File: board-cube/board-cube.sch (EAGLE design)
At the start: 164 parts, among them IC1 MSP430FR2110PW, IC2 LHA1+, IC3 MMZ09332BT1, Q1 BSS84, U1 TPS79933QDDCRQ1, U2 TPS79933QDDCRQ1, X1 BU-SMA-V, X10 BU-SMA-V, X11 BU-SMA-V, X12 BU-SMA-V, X13 BU-SMA-V, X14 BU-SMA-V, X15 BU-SMA-V, X16 BU-SMA-V, X17 BU-SMA-V, X2 BU-SMA-V, X3 BU-SMA-V, X4 BU-SMA-V, X5 BU-SMA-V, X6 BU-SMA-V, X7 BU-SMA-V, X8 BU-SMA-V, X9 BU-SMA-V

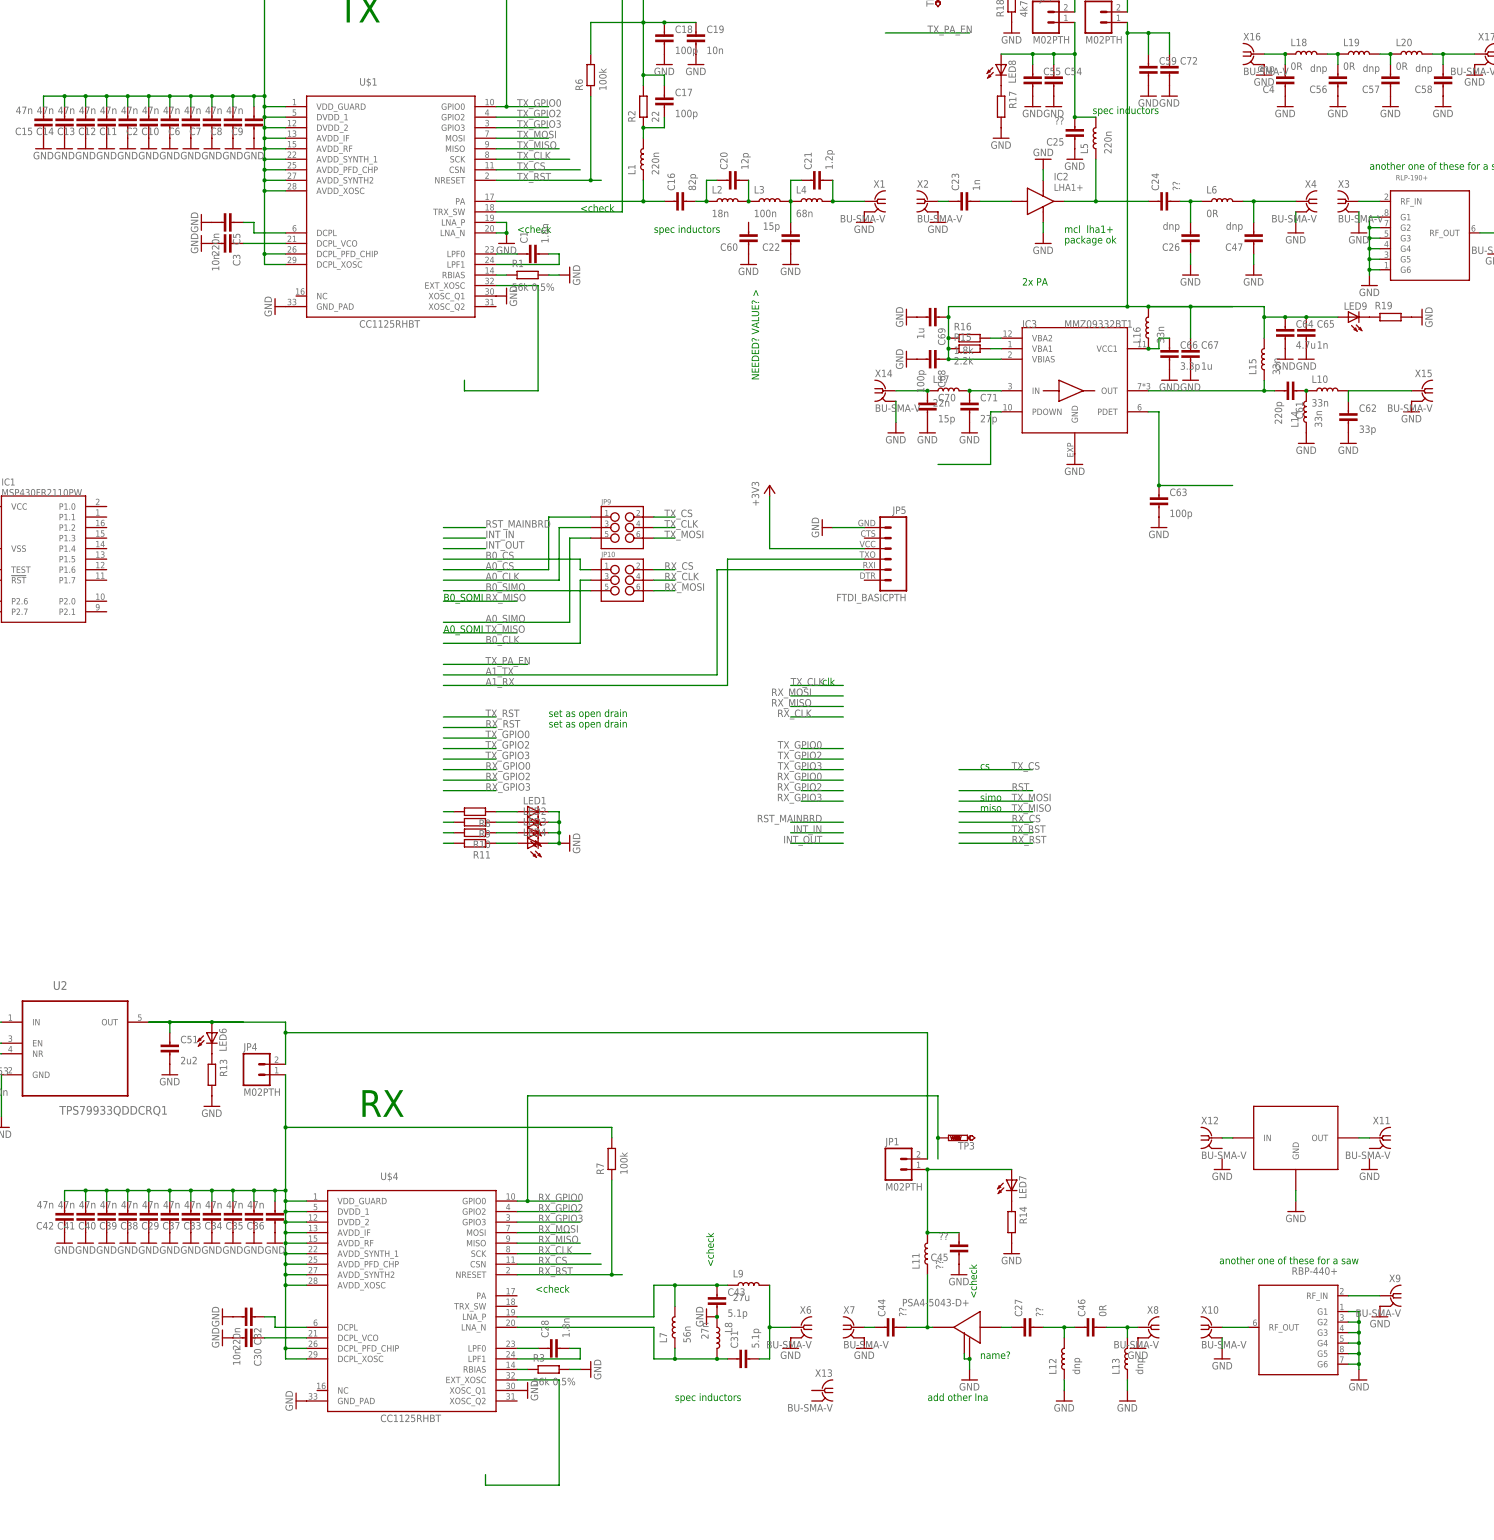
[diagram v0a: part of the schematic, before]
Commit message: adding tcxo and temp sensor
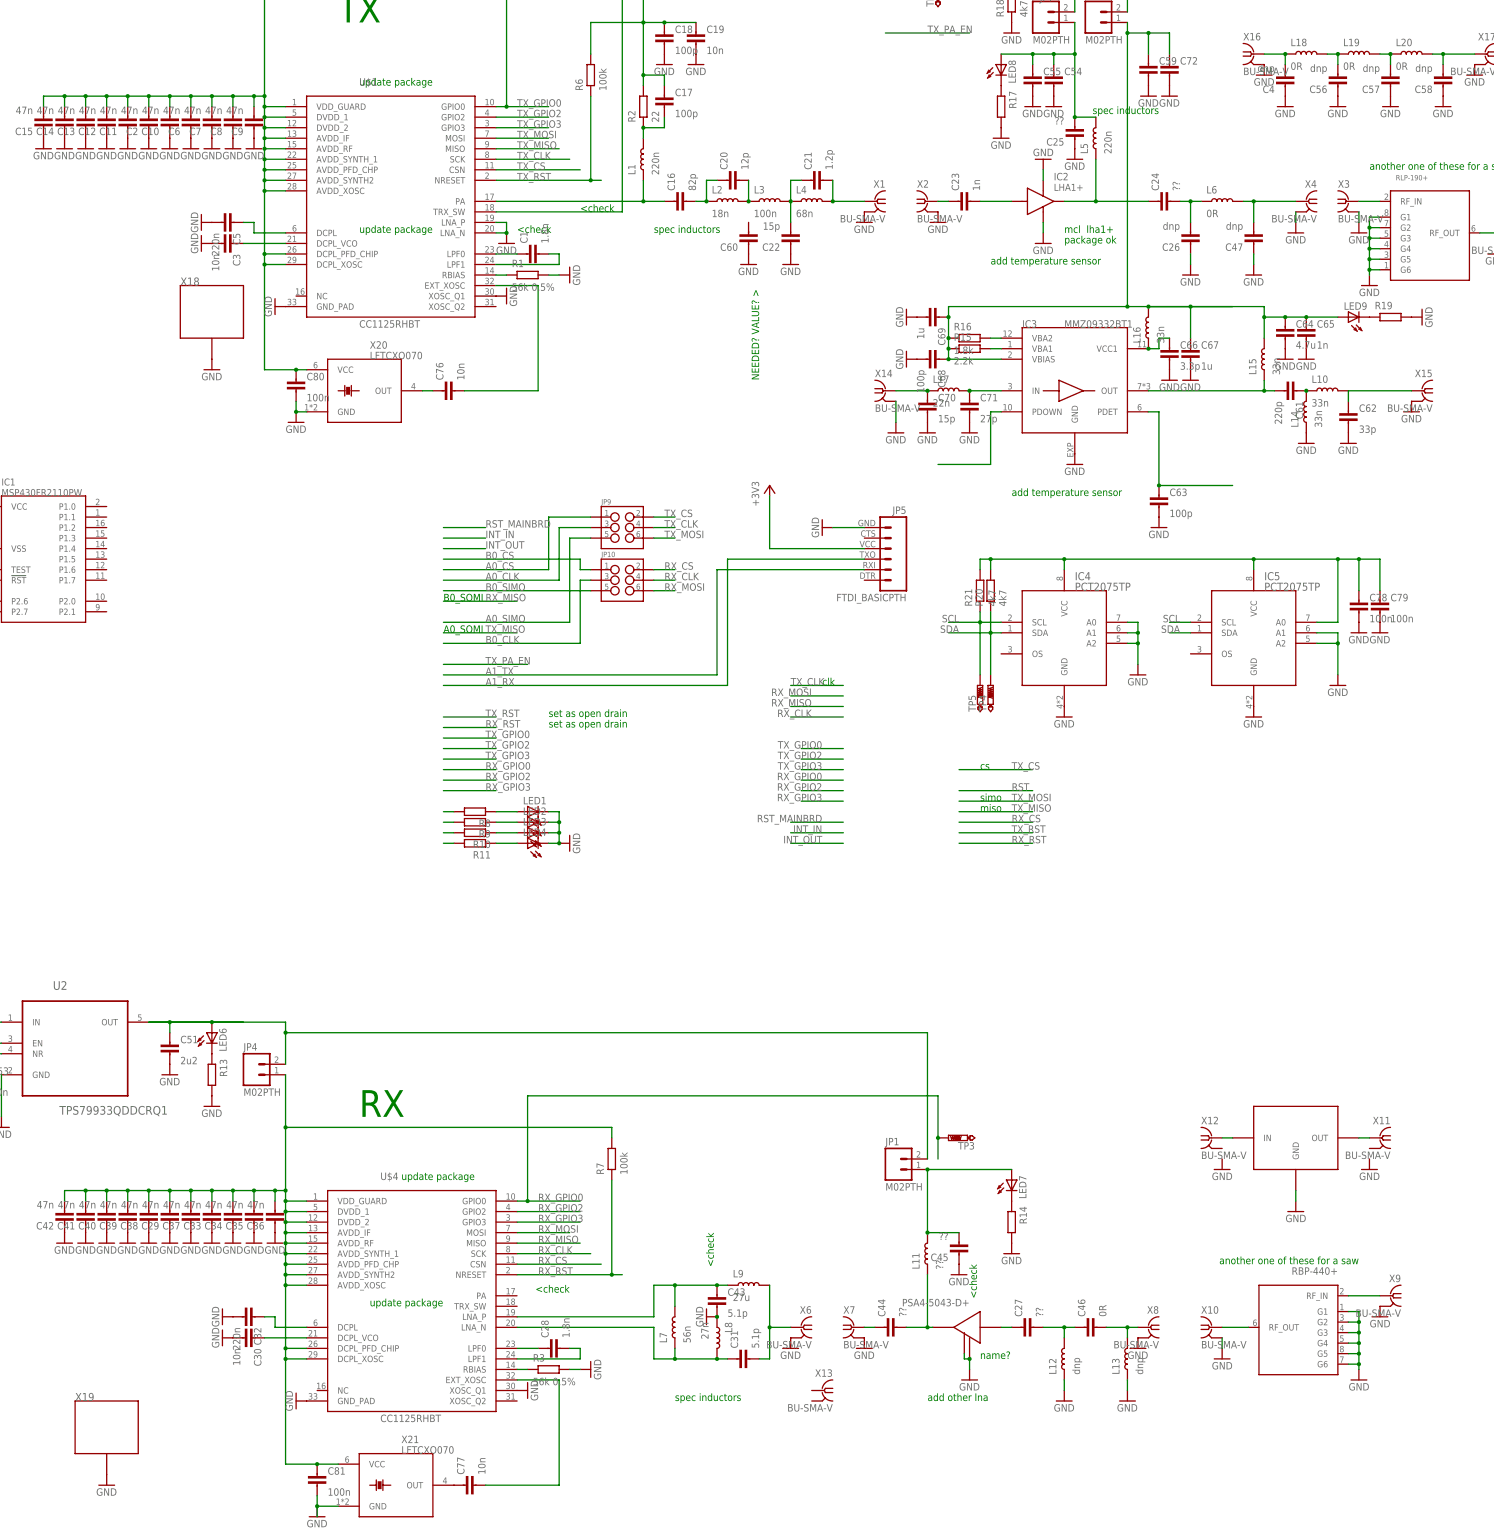
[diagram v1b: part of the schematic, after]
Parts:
- added C76, C77: 10n, passives-7351:CAPACITOR0603-N
- added C78, C79, C80, C81: 100n, passives-7351:CAPACITOR0603-N
- added IC4, IC5: PCT2075TP, CubeSat3:PCT2075TP
- added R20, R21: 4k7, passives-7351:RESISTOR0603-N
- added TP4, TP5: PTR1B1,27, testpad:PTR1B1,27
- added X18, X19: SHIELD-26X26, CubeSat3:SHIELD-26X26
- added X20, X21: LFTCXO070, CubeSat3:LFTCXO070
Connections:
- new net N$81: C76.1, X20.OUT
- new net N$82: C77.1, X21.OUT
- new net N$86: C78.1, C79.1, IC4.VCC, IC5.A0, IC5.VCC, R20.P$2, R21.P$2
- new net SCL: IC4.SCL, IC5.SCL, R21.P$1, TP5.TP
- new net SDA: IC4.SDA, IC5.SDA, R20.P$1, TP4.TP
- net GND: now also C78.2, C79.2, C80.2, C81.2, IC4.A0, IC4.A1, IC4.A2, IC4.GND, IC5.A1, IC5.A2, IC5.GND, X18.G, X19.G, X20.GND, X21.GND
- net N$36: now also C77.2
- net N$51: now also C80.1, X20.VCC
- net N$63: now also C81.1, X21.VCC
- net N$9: now also C76.2
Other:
- note added: "add temperature sensor"
- note added: "update package"
- note removed: "2x PA"

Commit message: updating footprints and values, changing msp watchdog part
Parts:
- removed IC1: MSP430FR2110PW, CubeSat3:MSP430FR2110PW
- added C82: (no value), passives-7351:CAPACITOR0603-N
- added IC6: MSP430FR2311PW, CubeSat3:MSP430FR2311PW
- added JP11: FTDI_BASICPTH, SparkFun-Connectors:FTDI_BASICPTH
- added JP8: (no value), SparkFun-Connectors:M04PTH
- added L21: 15n, passives-7351:INDUCTOR0603-N
- C60: value (none) -> 12p
- renumbered U$1 to IC7, U$3 to FL1, U$4 to IC8, U$6 to FL2, U$7 to FL3
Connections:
- new net N$83: IC6.TEST, JP8.4
- new net N$84: IC6.!RST, JP8.3
- new net N$85: IC6.P1.6, JP11.3
- new net N$87: IC6.P1.7, JP11.2
- new net N$88: C82.1, L21.P$2
- new net N$89: L21.P$1
- new net N$90: C82.2
- net GND: now also IC6.VSS, JP11.6, JP8.2; no longer IC1.VSS
- net N$21: now also C60.2
- net N$80: now also IC6.VCC, JP8.1; no longer IC1.VCC
- net SCL: now also IC6.P1.3
- net SDA: now also IC6.P1.2
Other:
- note added: "12p"
- note added: "150n"
- note added: "15n"
- note added: "18"
- note added: "22n"
- note added: "2p2"
- note added: "39p"
- note added: "43n"
- note added: "56n"
- note added: "56p"
- note added: "5p1"
- note added: "6p2"
- note added: "82n"
- note added: "^ needed?"
- note added: "dnp"
- note added: "for test board only"
- note added: "green: 144 MHz"
- note added: "green: 434 MHz"
- note added: "make consistant"
- note removed: "NEEDED? VALUE? >"
- note removed: "update package"

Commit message: added level shifter
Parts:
- removed JP10: (no value), SparkFun-Connectors:M03X22X3_SILK_MALE_PTH
- added C83, C84, C85, C86: 100n, passives-7351:CAPACITOR0603-N
- added IC1, IC9: TXB0108PW, cube-parts:TXB0108PW
- added JP12, JP13: M02PTH, SparkFun-Connectors:M02PTH
- added R22, R23: 10k, passives-7351:RESISTOR0603-N
- added R24: 0.2, passives-7351:RESISTOR0603-N
- JP9: value (none) -> M02PTH; device SparkFun-Connectors:M03X22X3_SILK_MALE_PTH -> SparkFun-Connectors:M02PTH
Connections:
- removed net A0_CLK: JP9.3
- removed net A0_CS: JP9.1
- removed net A0_SIMO: JP9.5
- removed net B0_CLK: JP10.3
- removed net B0_CS: JP10.1
- removed net B0_SIMO: JP10.5
- new net N$91: IC9.OE, JP13.1, R23.P$1
- new net N$92: C84.1, IC1.VCCB
- new net N$93: C86.1, IC9.VCCB
- new net N$94: C49.1, JP9.2, R24.P$2, U1.EN, U1.IN
- net +5V: now also JP9.1, R24.P$1; no longer C49.1, U1.EN, U1.IN
- net GND: now also C83.2, C84.2, C85.2, C86.2, IC1.GND, IC9.GND, JP12.2, JP13.2
- net N$51: now also C73.1, C74.1, C75.1, C83.1, IC1.VCCA, IC6.VCC, JP8.1, R22.P$2
- net N$63: now also C85.1, IC9.VCCA, R23.P$2
- net N$80: now also IC1.OE, JP12.1, R22.P$1; no longer C73.1, C74.1, C75.1, IC6.VCC, JP8.1
- net RX_CLK: no longer JP10.4
- net RX_CS: no longer JP10.2
- net RX_MOSI: no longer JP10.6
- net SCL: no longer IC6.P1.3
- net SDA: no longer IC6.P1.2
- net TX_CLK: no longer JP9.4
- net TX_CS: no longer JP9.2
- net TX_MOSI: no longer JP9.6
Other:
- note added: "power from same rail as tx"
- note added: "use OD signalling to main micro"
- note added: "use diode to prevent unintentional powering of tx rail"
- note added: "will probably need a IO buffer due to being able to power down one vcc rail"
- note removed: "for test board only"

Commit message: Fix PSA5043 LNA footprint.
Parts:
- renumbered U$5 to IC10
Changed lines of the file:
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@@
 <part name="GND35" library="supply1" deviceset="GND" device=""/>
 <part name="C44" library="passives-7351" deviceset="CAPACITOR" device="0603-N" value="??"/>
-<part name="U$5" library="CubeSat3" deviceset="LNA_COMMON" device=""/>
+<part name="IC10" library="CubeSat3" deviceset="LNA_COMMON" device=""/>
 <part name="C27" library="passives-7351" deviceset="CAPACITOR" device="0603-N" value="??"/>
 <part name="L11" library="passives-7351" deviceset="INDUCTOR" device="0603-N" value="??"/>
@@
 <instance part="GND35" gate="1" x="139.7" y="-226.06"/>
 <instance part="C44" gate="G$1" x="162.56" y="-220.98" rot="R90"/>
-<instance part="U$5" gate="G$1" x="182.88" y="-220.98" rot="MR0"/>
+<instance part="IC10" gate="G$1" x="182.88" y="-220.98" rot="MR0"/>
 <instance part="C27" gate="G$1" x="195.58" y="-220.98" rot="R90"/>
 <instance part="L11" gate="G$1" x="172.72" y="-203.2" rot="R90"/>
@@
 </segment>
 <segment>
-<pinref part="U$5" gate="G$1" pin="2"/>
+<pinref part="IC10" gate="G$1" pin="2"/>
 <wire x1="182.88" y1="-228.6" x2="182.88" y2="-231.14" width="0.1524" layer="91"/>
-<pinref part="U$5" gate="G$1" pin="4"/>
+<pinref part="IC10" gate="G$1" pin="4"/>
 <wire x1="182.88" y1="-228.6" x2="181.61" y2="-228.6" width="0.1524" layer="91"/>
 <wire x1="181.61" y1="-228.6" x2="181.61" y2="-227.33" width="0.1524" layer="91"/>
@@
 <pinref part="C44" gate="G$1" pin="2"/>
 <wire x1="172.72" y1="-220.98" x2="167.64" y2="-220.98" width="0.1524" layer="91"/>
-<pinref part="U$5" gate="G$1" pin="RF_OUT"/>
+<pinref part="IC10" gate="G$1" pin="RF_OUT"/>
 <wire x1="172.72" y1="-220.98" x2="173.99" y2="-220.98" width="0.1524" layer="91"/>
 <junction x="172.72" y="-220.98"/>
@@
 <segment>
 <pinref part="C27" gate="G$1" pin="1"/>
-<pinref part="U$5" gate="G$1" pin="RF_IN"/>
+<pinref part="IC10" gate="G$1" pin="RF_IN"/>
 <wire x1="193.04" y1="-220.98" x2="190.5" y2="-220.98" width="0.1524" layer="91"/>
 </segment>

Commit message: most digital signals wired up
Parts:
- removed X13: BU-SMA-V, con-coax:BU-SMA-V
- added C87: 100n, passives-7351:CAPACITOR0603-N
- added Q2: BSS123, transistor-small-signal:BSS123
- added Q3: BSS84, transistor-small-signal:BSS84
- added R25: 10k, passives-7351:RESISTOR0603-N
- added R26: 100k, passives-7351:RESISTOR0603-N
- added TP6: PTR1B1,27, testpad:PTR1B1,27
- added U3: 74LVC1G08, SparkFun-DigitalIC:SN74LVC1G08
- JP5: value FTDI_BASICPTH -> M02PTH; device SparkFun-Connectors:FTDI_BASICPTH -> SparkFun-Connectors:M02PTH
- R18: value 4k7 -> 10k
- TP1, TP2, TP3: value PTR1PAD1-20 -> PTR1B1,27; device testpad:PTR1PAD1-20 -> testpad:PTR1B1,27
- U1, U2: value TPS79933QDDCRQ1 -> TPS79930QDDCRQ1
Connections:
- removed net +3V3: JP5.4
- removed net A1_RX: JP5.3
- removed net A1_TX: JP5.2
- removed net N$89: L21.P$1
- new net N$101: IC9.B8
- new net N$102: IC1.B1
- new net N$103: IC1.B2
- new net N$104: IC1.B3
- new net N$105: IC1.B4
- new net N$106: IC1.B5
- new net N$107: IC1.B6
- new net N$108: IC1.B7
- new net N$109: IC1.B8
- new net N$110: IC9.B7
- new net N$111: IC9.B6
- new net N$112: IC9.B5
- new net N$113: IC9.B4
- new net N$114: IC9.B3
- new net N$115: IC9.B2
- new net N$116: IC9.B1
- new net N$117: Q2.G, R18.P$2, U3.Y
- new net WDT_ACK: IC6.P1.5
- new net WDT_ERR: IC1.A8, IC6.P1.4
- new net WDT_PA_EN: IC6.P1.0, TP6.TP, U3.B
- net +5V: now also JP7.1
- net GND: now also C87.2, IC3.PDOWN, Q2.S, U3.GND; no longer JP5.6
- net N$24: now also LED9.A
- net N$49: now also C82.2; no longer C31.2, L9.P$2
- net N$51: now also C87.1, U3.+V
- net N$52: now also JP5.2
- net N$53: now also JP5.1, Q3.S, R26.P$2; no longer JP1.2
- net N$6: now also JP7.2
- net N$62: now also Q2.D; no longer JP7.1
- net N$69: now also C49.1, JP9.2, R24.P$2, R25.P$2, U1.IN; no longer JP7.2, R18.P$2
- net N$75: now also JP1.2, Q3.D; no longer IC3.PDOWN
- net N$90: now also C31.2, L21.P$1, L9.P$2; no longer C82.2
- net N$94: now also R25.P$1; no longer C49.1, JP9.2, R24.P$2, U1.IN
- net RX_CLK: now also IC9.A6
- net RX_CS: now also IC9.A7
- net RX_GPIO0: now also IC9.A1; no longer TP3.TP
- net RX_GPIO2: now also IC9.A2
- net RX_GPIO3: now also IC9.A3, Q3.G, R26.P$1, TP3.TP
- net RX_MISO: now also IC9.A5
- net RX_MOSI: now also IC9.A4
- net RX_RST: now also IC9.A8
- net TX_CLK: now also IC1.A6
- net TX_CS: now also IC1.A7, IC6.P1.1
- net TX_GPIO0: now also IC1.A1, IC6.P1.3; no longer TP2.TP
- net TX_GPIO2: now also IC1.A2
- net TX_GPIO3: now also TP2.TP, U3.A
- net TX_MISO: now also IC1.A5
- net TX_MOSI: now also IC1.A4
- net TX_RST: now also IC1.A3, IC6.P1.2
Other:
- note removed: "A0_SOMI"
- note removed: "B0_SOMI"
- note removed: "^ needed?"
- note removed: "add other lna"
- note removed: "add temperature sensor"
- note removed: "clk"
- note removed: "cs"
- note removed: "miso"
- note removed: "name?"
- note removed: "package ok"
- note removed: "power from same rail as tx"
- note removed: "set as open drain"
- note removed: "simo"
- note removed: "use OD signalling to main micro"
- note removed: "use diode to prevent unintentional powering of tx rail"
- note removed: "will probably need a IO buffer due to being able to power down one vcc rail"
- moved on the sheet: C27, C28, C29, C30, C31, C32, C33, C34, C35, C36, C37, C38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
